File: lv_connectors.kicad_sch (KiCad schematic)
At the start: 31 parts, among them J10 Conn_01x10, J2 Conn_01x04, J3 Conn_01x04, J4 Conn_01x04, J6 Conn_01x02, J7 Conn_01x04, J9 Conn_01x02, Q5 PMOS, Q6 PMOS, U15 TBA1-1211E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

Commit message: Misc.
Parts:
- removed J9: Conn_01x02, wuerth_conn:66200211024, symbol Connector_Generic:Conn_01x02
- added J11, J12, J13, J8, J9: Conn_01x04, symbol Connector_Generic:Conn_01x04
- added J14: Conn_01x04, wuerth_conn:66200411022, symbol Connector_Generic:Conn_01x04
- added J15: Conn_01x10, symbol Connector_Generic:Conn_01x10
- D4, D5: Mouser (none) -> 726-ESD131B1W0201E63
- J10: Mouser (none) -> 710-61201022021
- J2, J3, J4, J7: Mouser 66200411022 -> 710-66200421022
- R86: value 7k5 -> e
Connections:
- net +24V: now also J14.1 (Pin_1)
- net +5V: now also J14.3 (Pin_3)
- net GND: now also J14.4 (Pin_4)
- new net +12V: J14.2 (Pin_2)

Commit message: TSAL Rev 0.2
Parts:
- R85: value 30k -> 30k
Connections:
- net +24V: now also Q5.3 (S), Q6.3 (S); no longer Q5.1 (D), Q6.1 (D)
- net at D4.2 (A2), J7.2 (Pin_2): now also Q6.1 (D); no longer Q6.3 (S)
- net at D5.2 (A2), J7.1 (Pin_1): now also Q5.1 (D); no longer Q5.3 (S)
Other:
- note added: "Fixed PMOS orientation"
- moved on the sheet: J13, Q5, Q6
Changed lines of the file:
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@@
 		(title "TSAL")
 		(date "2024-07-11")
-		(rev "V0.1")
+		(rev "V0.2")
 		(company "Team RPM - UAS Münster")
 		(comment 1 "Luca Sapion")
@@
 		)
 	)
+	(text "Fixed PMOS orientation "
+		(exclude_from_sim no)
+		(at 48.006 168.402 0)
+		(effects
+			(font
+				(size 1.27 1.27)
+			)
+		)
+	)
 	(text "AIR"
 		(exclude_from_sim no)
@@
 		)
 	)
+	(text "Fixed PMOS orientation "
+		(exclude_from_sim no)
+		(at 46.99 137.16 0)
+		(effects
+			(font
+				(size 1.27 1.27)
+			)
+		)
+	)
 	(label "SDC"
 		(at 41.91 96.52 0)
@@
 	(symbol
 		(lib_id "Simulation_SPICE:PMOS")
-		(at 63.5 172.72 0)
-		(mirror y)
+		(at 63.5 172.72 180)
 		(unit 1)
 		(exclude_from_sim no)
@@
 		(on_board yes)
 		(dnp no)
-		(fields_autoplaced yes)
 		(property "Reference" "Q6"
-			(at 57.15 171.4499 0)
+			(at 57.15 173.9901 0)
 			(effects
 				(font
@@
 		)
 		(property "Value" "PMOS"
-			(at 57.15 173.9899 0)
+			(at 57.15 171.4501 0)
 			(effects
 				(font
@@
 		)
 		(property "Footprint" "Package_TO_SOT_SMD:SOT-23-3"
-			(at 58.42 170.18 0)
+			(at 58.42 175.26 0)
 			(effects
 				(font
@@
 		)
 		(property "Datasheet" "https://ngspice.sourceforge.io/docs/ngspice-html-manual/manual.xhtml#cha_MOSFETs"
-			(at 63.5 185.42 0)
+			(at 63.5 160.02 0)
 			(effects
 				(font
@@
 		)
 		(property "Sim.Device" "PMOS"
-			(at 63.5 189.865 0)
+			(at 63.5 155.575 0)
 			(effects
 				(font
@@
 		)
 		(property "Sim.Type" "VDMOS"
-			(at 63.5 191.77 0)
+			(at 63.5 153.67 0)
 			(effects
 				(font
@@
 		)
 		(property "Sim.Pins" "1=D 2=G 3=S"
-			(at 63.5 187.96 0)
+			(at 63.5 157.48 0)
 			(effects
 				(font
@@
 	(symbol
 		(lib_id "Connector_Generic:Conn_01x04")
-		(at 116.84 152.4 0)
+		(at 120.65 153.67 0)
 		(mirror y)
 		(unit 1)
@@
 		(dnp yes)
 		(property "Reference" "J13"
-			(at 115.062 144.526 0)
+			(at 118.872 145.796 0)
 			(effects
 				(font
@@
 		)
 		(property "Value" "Conn_01x04"
-			(at 115.062 147.066 0)
+			(at 118.872 148.336 0)
 			(effects
 				(font
@@
 		)
 		(property "Footprint" ""
-			(at 116.84 152.4 0)
+			(at 120.65 153.67 0)
 			(effects
 				(font
@@
 		)
 		(property "Datasheet" "~"
-			(at 116.84 152.4 0)
+			(at 120.65 153.67 0)
 			(effects
 				(font
@@
 		)
 		(property "Description" "Generic connector, single row, 01x04, script generated (kicad-library-utils/schlib/autogen/connector/)"
-			(at 116.84 152.4 0)
+			(at 120.65 153.67 0)
 			(effects
 				(font
@@
 		)
 		(property "Mouser" "710-662004113322 "
-			(at 116.84 152.4 0)
+			(at 120.65 153.67 0)
 			(effects
 				(font
@@
 		)
 		(property "resistor datasheet" ""
-			(at 116.84 152.4 0)
+			(at 120.65 153.67 0)
 			(effects
 				(font
@@
 			)
 		)
-		(property "Value" "30k	"
+		(property "Value" "30k"
 			(at 62.23 101.5999 0)
 			(effects
@@
 	(symbol
 		(lib_id "Simulation_SPICE:PMOS")
-		(at 63.5 142.24 0)
-		(mirror y)
+		(at 63.5 142.24 180)
 		(unit 1)
 		(exclude_from_sim no)
@@
 		(on_board yes)
 		(dnp no)
-		(fields_autoplaced yes)
 		(property "Reference" "Q5"
-			(at 57.15 140.9699 0)
+			(at 57.15 143.5101 0)
 			(effects
 				(font
@@
 		)
 		(property "Value" "PMOS"
-			(at 57.15 143.5099 0)
+			(at 57.15 140.9701 0)
 			(effects
 				(font
@@
 		)
 		(property "Footprint" "Package_TO_SOT_SMD:SOT-23-3"
-			(at 58.42 139.7 0)
+			(at 58.42 144.78 0)
 			(effects
 				(font
@@
 		)
 		(property "Datasheet" "https://ngspice.sourceforge.io/docs/ngspice-html-manual/manual.xhtml#cha_MOSFETs"
-			(at 63.5 154.94 0)
+			(at 63.5 129.54 0)
 			(effects
 				(font
@@
 		)
 		(property "Sim.Device" "PMOS"
-			(at 63.5 159.385 0)
+			(at 63.5 125.095 0)
 			(effects
 				(font
@@
 		)
 		(property "Sim.Type" "VDMOS"
-			(at 63.5 161.29 0)
+			(at 63.5 123.19 0)
 			(effects
 				(font
@@
 		)
 		(property "Sim.Pins" "1=D 2=G 3=S"
-			(at 63.5 157.48 0)
+			(at 63.5 127 0)
 			(effects
 				(font

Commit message: Added Seperate Project
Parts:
- removed D4: ESD, Diode_SMD:Infineon_SG-WLL-2-3_0.58x0.28_P0.36mm, symbol Diode:ESD131-B1-W0201
- removed J13: Conn_01x04, symbol Connector_Generic:Conn_01x04
- removed J7: Conn_01x04, wuerth_conn:66200411022, symbol Connector_Generic:Conn_01x04
- removed Q6: PMOS, Package_TO_SOT_SMD:SOT-23-3, symbol Simulation_SPICE:PMOS
- removed R79: 200R, Resistor_SMD:R_0603_1608Metric, symbol Device:R
- removed R80: 10k, Resistor_SMD:R_0603_1608Metric, symbol Device:R
- added J7: Conn_01x02, wuerth_conn:66200211024, symbol Connector_Generic:Conn_01x02
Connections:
- net GND: now also J7.2 (Pin_2)
- net at D5.2 (A2), Q5.1 (D): now also J7.1 (Pin_1)
- no-connect marks 1 -> 0

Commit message: Added Sub project
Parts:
- added H1, H2, H3, H4, H5: MountingHole, MountingHole:MountingHole_3.2mm_M3, symbol Mechanical:MountingHole
- J10: footprint (none) -> Connector_IDC:IDC-Header_2x05_P2.54mm_Latch6.5mm_Vertical

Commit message: Connector Updated
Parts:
- J14, J2, J3, J4: footprint wuerth_conn:66200411022 -> wuerth_conn:66200421022
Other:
- note added: "2x2 Conn"
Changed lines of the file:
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@@
 		)
 	)
+	(text "2x2 Conn\n"
+		(exclude_from_sim no)
+		(at 70.104 78.232 0)
+		(effects
+			(font
+				(size 1.27 1.27)
+			)
+		)
+	)
 	(text "DC-DC Converter"
 		(exclude_from_sim no)
@@
 		)
 	)
+	(text "2x2 Conn\n"
+		(exclude_from_sim no)
+		(at 16.002 33.528 0)
+		(effects
+			(font
+				(size 1.27 1.27)
+			)
+		)
+	)
+	(text "2x2 Conn\n"
+		(exclude_from_sim no)
+		(at 18.288 78.486 0)
+		(effects
+			(font
+				(size 1.27 1.27)
+			)
+		)
+	)
 	(text "TSAL LEDs"
 		(exclude_from_sim no)
@@
 		)
 	)
+	(text "2x2 Conn\n"
+		(exclude_from_sim no)
+		(at 17.018 54.356 0)
+		(effects
+			(font
+				(size 1.27 1.27)
+			)
+		)
+	)
 	(text "Shutdown Circuit"
 		(exclude_from_sim no)
@@
 			)
 		)
-		(property "Footprint" "wuerth_conn:66200411022"
+		(property "Footprint" "wuerth_conn:66200421022"
 			(at 17.78 25.4 0)
 			(effects
@@
 			)
 		)
+		(property "resistor datasheet" ""
+			(at 17.78 25.4 0)
+			(effects
+				(font
+					(size 1.27 1.27)
+				)
+			)
+		)
 		(pin "2"
 		)
@@
 			)
 		)
-		(property "Footprint" "wuerth_conn:66200411022"
+		(property "Footprint" "wuerth_conn:66200421022"
 			(at 17.78 45.72 0)
 			(effects
@@
 			)
 		)
+		(property "resistor datasheet" ""
+			(at 17.78 45.72 0)
+			(effects
+				(font
+					(size 1.27 1.27)
+				)
+			)
+		)
 		(pin "2"
 		)
@@
 			)
 		)
-		(property "Footprint" "wuerth_conn:66200411022"
+		(property "Footprint" "wuerth_conn:66200421022"
 			(at 17.78 69.85 0)
 			(effects
@@
 			)
 		)
-		(property "Footprint" "wuerth_conn:66200411022"
+		(property "Footprint" "wuerth_conn:66200421022"
 			(at 68.58 69.85 0)
 			(effects

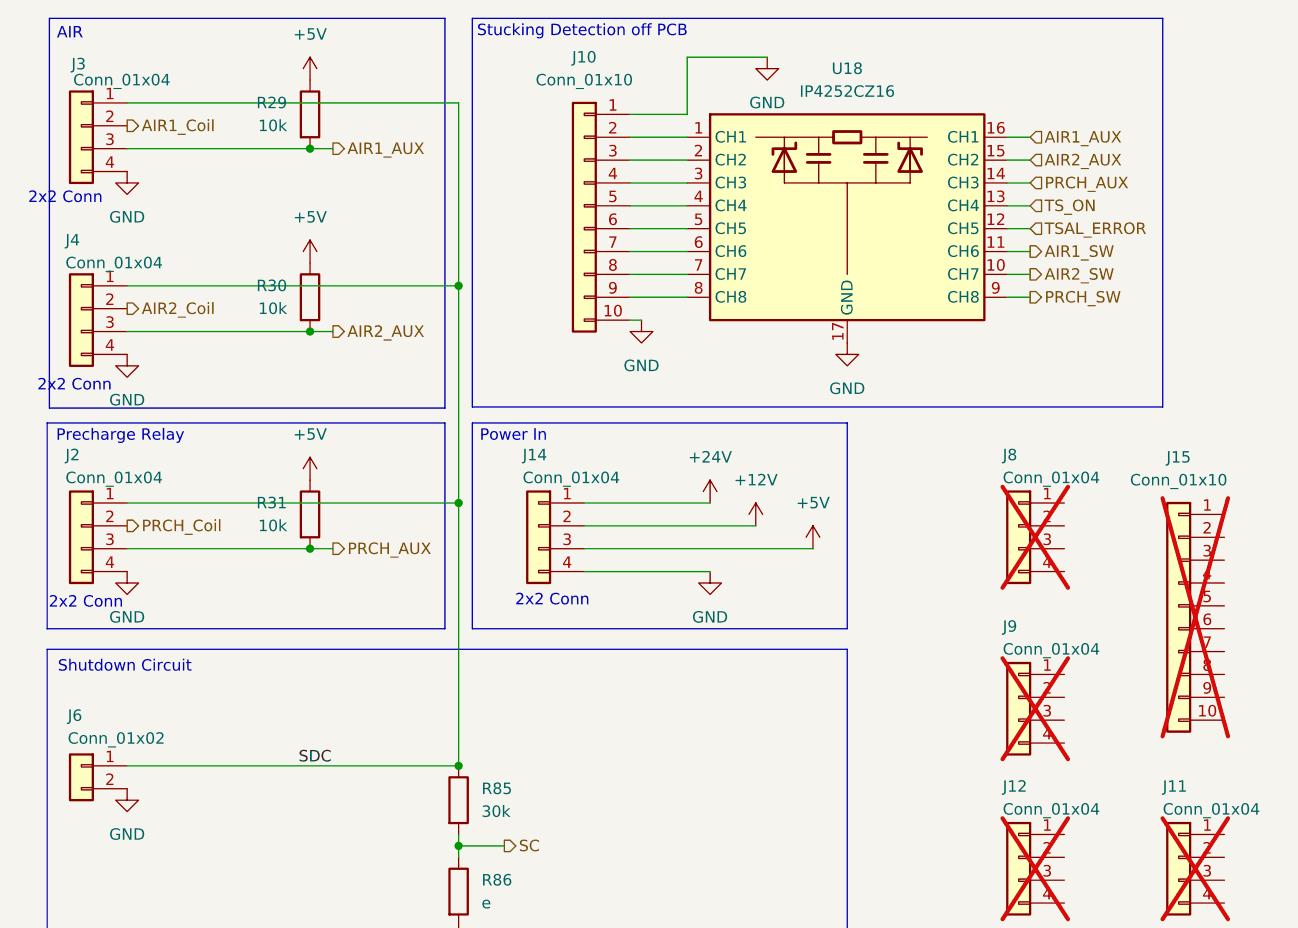
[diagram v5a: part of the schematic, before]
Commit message: Routing of AIR Relay
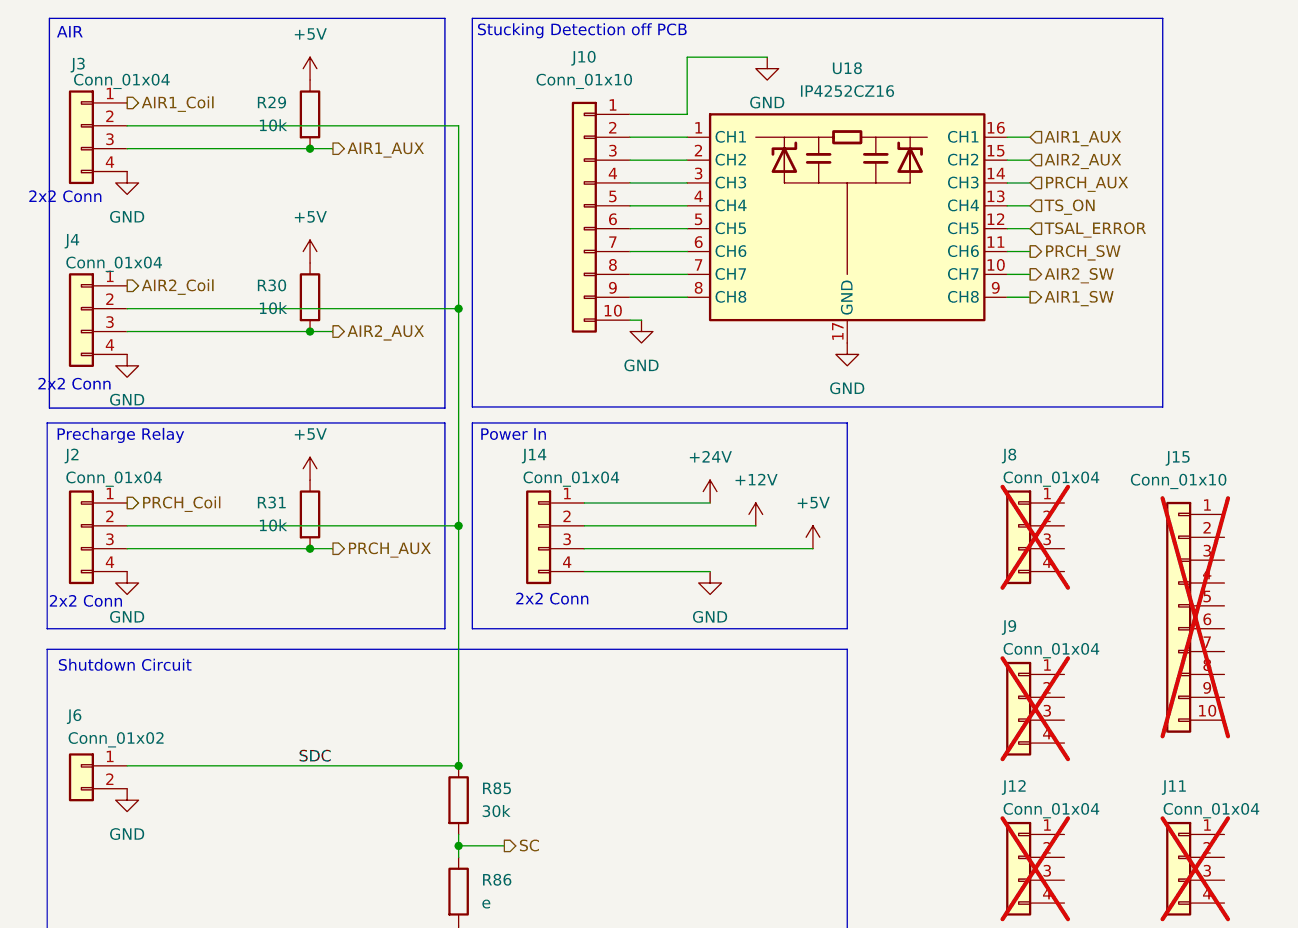
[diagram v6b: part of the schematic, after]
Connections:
- net AIR1_Coil: now also J3.1 (Pin_1); no longer J3.2 (Pin_2)
- net AIR1_SW: now also U18.9 (CH8); no longer U18.11 (CH6)
- net AIR2_Coil: now also J4.1 (Pin_1); no longer J4.2 (Pin_2)
- net PRCH_Coil: now also J2.1 (Pin_1); no longer J2.2 (Pin_2)
- net PRCH_SW: now also U18.11 (CH6); no longer U18.9 (CH8)
- net SDC: now also J2.2 (Pin_2), J3.2 (Pin_2), J4.2 (Pin_2); no longer J2.1 (Pin_1), J3.1 (Pin_1), J4.1 (Pin_1)
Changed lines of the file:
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@@
+	)
+	(junction
+		(at 59.69 69.85)
+		(diameter 0)
+		(color 0 0 0 0)
 	)
 	(junction
@@
 	)
 	(junction
-		(at 59.69 67.31)
-		(diameter 0)
-		(color 0 0 0 0)
-	)
-	(junction
 		(at 59.69 105.41)
 		(diameter 0)
@@
 	)
 	(junction
-		(at 59.69 43.18)
-		(diameter 0)
-		(color 0 0 0 0)
-	)
-	(junction
 		(at 228.6 72.39)
 		(diameter 0)
@@
 		(color 0 0 0 0)
 	)
+	(junction
+		(at 59.69 45.72)
+		(diameter 0)
+		(color 0 0 0 0)
+	)
 	(wire
 		(pts
@@
 	(wire
 		(pts
+			(xy 59.69 25.4) (xy 22.86 25.4)
+		)
+		(stroke
+			(width 0)
+			(type default)
+		)
+	)
+	(wire
+		(pts
 			(xy 73.66 67.31) (xy 87.63 67.31)
 		)
@@
 	(wire
 		(pts
+			(xy 59.69 45.72) (xy 59.69 69.85)
+		)
+		(stroke
+			(width 0)
+			(type default)
+		)
+	)
+	(wire
+		(pts
 			(xy 72.39 132.08) (xy 60.96 132.08)
 		)
@@
 	(wire
 		(pts
-			(xy 59.69 22.86) (xy 22.86 22.86)
-		)
-		(stroke
-			(width 0)
-			(type default)
-		)
-	)
-	(wire
-		(pts
 			(xy 78.74 36.83) (xy 85.09 36.83)
 		)
@@
 	(wire
 		(pts
+			(xy 59.69 25.4) (xy 59.69 45.72)
+		)
+		(stroke
+			(width 0)
+			(type default)
+		)
+	)
+	(wire
+		(pts
 			(xy 248.92 72.39) (xy 254 72.39)
 		)
@@
 	(wire
 		(pts
-			(xy 59.69 22.86) (xy 59.69 43.18)
-		)
-		(stroke
-			(width 0)
-			(type default)
-		)
-	)
-	(wire
-		(pts
 			(xy 207.01 43.18) (xy 219.71 43.18)
 		)
@@
 	(wire
 		(pts
+			(xy 22.86 69.85) (xy 59.69 69.85)
+		)
+		(stroke
+			(width 0)
+			(type default)
+		)
+	)
+	(wire
+		(pts
 			(xy 123.19 44.45) (xy 120.65 44.45)
 		)
@@
 	(wire
 		(pts
+			(xy 22.86 45.72) (xy 59.69 45.72)
+		)
+		(stroke
+			(width 0)
+			(type default)
+		)
+	)
+	(wire
+		(pts
 			(xy 241.3 76.2) (xy 228.6 76.2)
 		)
@@
 	(wire
 		(pts
-			(xy 22.86 43.18) (xy 59.69 43.18)
-		)
-		(stroke
-			(width 0)
-			(type default)
-		)
-	)
-	(wire
-		(pts
-			(xy 59.69 67.31) (xy 59.69 43.18)
-		)
-		(stroke
-			(width 0)
-			(type default)
-		)
-	)
-	(wire
-		(pts
 			(xy 43.18 27.94) (xy 22.86 27.94)
 		)
@@
 	(wire
 		(pts
+			(xy 59.69 69.85) (xy 59.69 96.52)
+		)
+		(stroke
+			(width 0)
+			(type default)
+		)
+	)
+	(wire
+		(pts
 			(xy 254 72.39) (xy 260.35 72.39)
 		)
@@
 	(wire
 		(pts
-			(xy 22.86 67.31) (xy 59.69 67.31)
-		)
-		(stroke
-			(width 0)
-			(type default)
-		)
-	)
-	(wire
-		(pts
 			(xy 53.34 147.32) (xy 29.21 147.32)
 		)
@@
 		(pts
 			(xy 53.34 147.32) (xy 60.96 147.32)
-		)
-		(stroke
-			(width 0)
-			(type default)
-		)
-	)
-	(wire
-		(pts
-			(xy 59.69 67.31) (xy 59.69 96.52)
 		)
 		(stroke
@@
 	(hierarchical_label "AIR1_Coil"
 		(shape output)
-		(at 22.86 25.4 0)
+		(at 22.86 22.86 0)
 		(fields_autoplaced yes)
 		(effects
@@
 		)
 	)
+	(hierarchical_label "PRCH_SW"
+		(shape output)
+		(at 123.19 39.37 0)
+		(fields_autoplaced yes)
+		(effects
+			(font
+				(size 1.27 1.27)
+			)
+			(justify left)
+		)
+	)
 	(hierarchical_label "PRCH_Coil"
 		(shape output)
-		(at 22.86 69.85 0)
+		(at 22.86 67.31 0)
+		(fields_autoplaced yes)
+		(effects
+			(font
+				(size 1.27 1.27)
+			)
+			(justify left)
+		)
+	)
+	(hierarchical_label "AIR1_SW"
+		(shape output)
+		(at 123.19 44.45 0)
 		(fields_autoplaced yes)
 		(effects
@@
 	(hierarchical_label "AIR2_Coil"
 		(shape output)
-		(at 22.86 45.72 0)
+		(at 22.86 43.18 0)
 		(fields_autoplaced yes)
 		(effects
@@
 		(fields_autoplaced yes)
 		(effects
-			(font
-				(size 1.27 1.27)
-			)
-			(justify left)
-		)
-	)
-	(hierarchical_label "AIR1_SW"
-		(shape output)
-		(at 123.19 39.37 0)
-		(fields_autoplaced yes)
-		(effects
-			(font
-				(size 1.27 1.27)
-			)
-			(justify left)
-		)
-	)
-	(hierarchical_label "PRCH_SW"
-		(shape output)
-		(at 123.19 44.45 0)
-		(fields_autoplaced yes)
-		(effects

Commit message: misc
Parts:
- removed J14: Conn_01x04, wuerth_conn:66200421022, symbol Connector_Generic:Conn_01x04
- added J5: Conn_01x02, wuerth_conn:66200211024, symbol Connector_Generic:Conn_01x02
- J6: footprint wuerth_conn:66200211024 -> Connector_AMASS:AMASS_XT60-F_1x02_P7.20mm_Vertical
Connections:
- net +24V: now also J5.1 (Pin_1)
- net GND: now also J5.2 (Pin_2)
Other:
- note removed: "2x2 Conn"
